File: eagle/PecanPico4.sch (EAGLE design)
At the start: 108 parts, among them IC2 61201, IC3 SI4463/4, IC4 ATMEGA328P-AU, IC5 UBLOX_MAX-6, IC6 61201, J1 AVR_SPI_PRG_6PTH, U1 EEPROM-I2CSMD, X1 MC-921

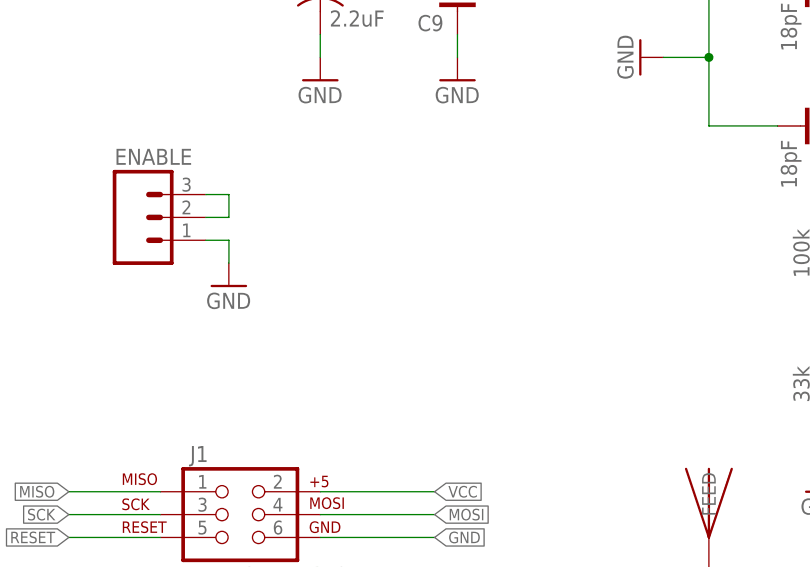
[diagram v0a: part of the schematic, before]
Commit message: Added breakout for I2C, ADC2/3
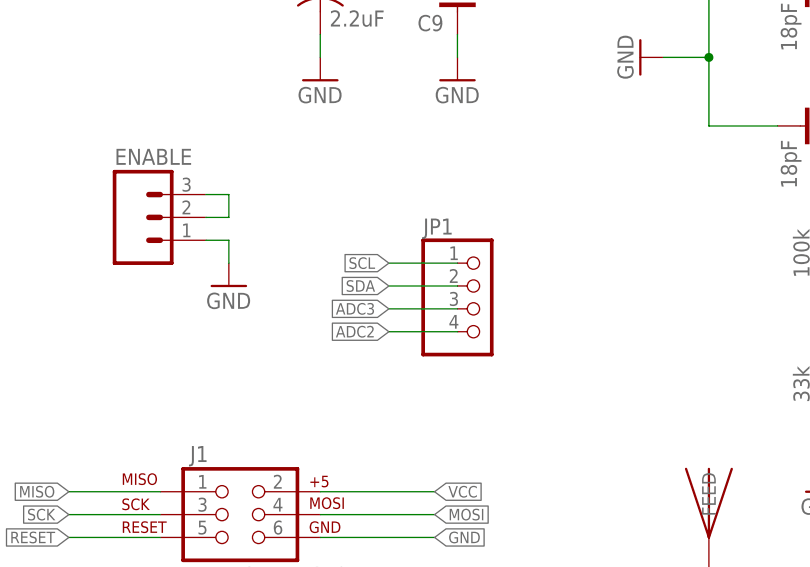
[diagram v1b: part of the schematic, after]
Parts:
- added JP1: (no value), pinhead:PINHD-1X4
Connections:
- new net N$18: JP1.1
- new net N$37: JP1.2
- new net N$38: JP1.3
- new net N$39: JP1.4
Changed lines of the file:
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@@
 <?xml version="1.0" encoding="utf-8"?>
 <!DOCTYPE eagle SYSTEM "eagle.dtd">
-<eagle version="6.4">
+<eagle version="6.5.0">
 <drawing>
 <settings>
@@
 <part name="GND51" library="SparkFun" deviceset="GND" device=""/>
 <part name="SERIAL" library="SparkFun-Connectors" deviceset="M03" device="PTH"/>
+<part name="JP1" library="pinhead" deviceset="PINHD-1X4" device=""/>
 </parts>
 <sheets>
@@
 <instance part="GND51" gate="1" x="358.14" y="279.4" rot="R270"/>
 <instance part="SERIAL" gate="G$1" x="340.36" y="35.56" rot="R90"/>
+<instance part="JP1" gate="A" x="205.74" y="111.76"/>
 </instances>
 <busses>
@@
 <wire x1="160.02" y1="53.34" x2="157.48" y2="53.34" width="0.1524" layer="91"/>
 <label x="157.48" y="53.34" size="1.27" layer="95" rot="R180" xref="yes"/>
+<label x="195.58" y="114.3" size="1.27" layer="95" rot="R180" xref="yes"/>
 </segment>
 <segment>
@@
 <wire x1="190.5" y1="53.34" x2="193.04" y2="53.34" width="0.1524" layer="91"/>
 <label x="193.04" y="53.34" size="1.27" layer="95" xref="yes"/>
+<label x="195.58" y="116.84" size="1.27" layer="95" rot="R180" xref="yes"/>
 </segment>
 <segment>
@@
 <wire x1="322.58" y1="167.64" x2="340.36" y2="167.64" width="0.1524" layer="91"/>
 <label x="340.36" y="167.64" size="1.27" layer="95" xref="yes"/>
+<label x="195.58" y="109.22" size="1.27" layer="95" rot="R180" xref="yes"/>
 </segment>
 </net>
@@
 <wire x1="322.58" y1="165.1" x2="340.36" y2="165.1" width="0.1524" layer="91"/>
 <label x="340.36" y="165.1" size="1.27" layer="95" xref="yes"/>
+<label x="195.58" y="111.76" size="1.27" layer="95" rot="R180" xref="yes"/>
 </segment>
 </net>
@@
 </segment>
 </net>
+<net name="N$18" class="0">
+<segment>
+<pinref part="JP1" gate="A" pin="1"/>
+<wire x1="195.58" y1="116.84" x2="203.2" y2="116.84" width="0.1524" layer="91"/>
+</segment>
+</net>
+<net name="N$37" class="0">
+<segment>
+<pinref part="JP1" gate="A" pin="2"/>
+<wire x1="195.58" y1="114.3" x2="203.2" y2="114.3" width="0.1524" layer="91"/>
+</segment>
+</net>
+<net name="N$38" class="0">
+<segment>
+<pinref part="JP1" gate="A" pin="3"/>
+<wire x1="195.58" y1="111.76" x2="203.2" y2="111.76" width="0.1524" layer="91"/>
+</segment>
+</net>
+<net name="N$39" class="0">
+<segment>
+<pinref part="JP1" gate="A" pin="4"/>
+<wire x1="195.58" y1="109.22" x2="203.2" y2="109.22" width="0.1524" layer="91"/>
+</segment>
+</net>
